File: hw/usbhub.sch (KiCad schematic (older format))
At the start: 0 parts

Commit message: Add more
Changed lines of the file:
@@
 $Descr A4 11693 8268
 encoding utf-8
-Sheet 1 2
+Sheet 1 4
 Title ""
 Date ""
@@
 F1 "USB2517.sch" 50
 $EndSheet
+$Sheet
+S 5550 2750 1550 2450
+U 5B992EC8
+F0 "USBPorts" 50
+F1 "USBPorts.sch" 50
+$EndSheet
+$Sheet
+S 7550 2750 1250 2400
+U 5B9586FD
+F0 "MCU" 50
+F1 "MCU.sch" 50
+$EndSheet
 $EndSCHEMATC

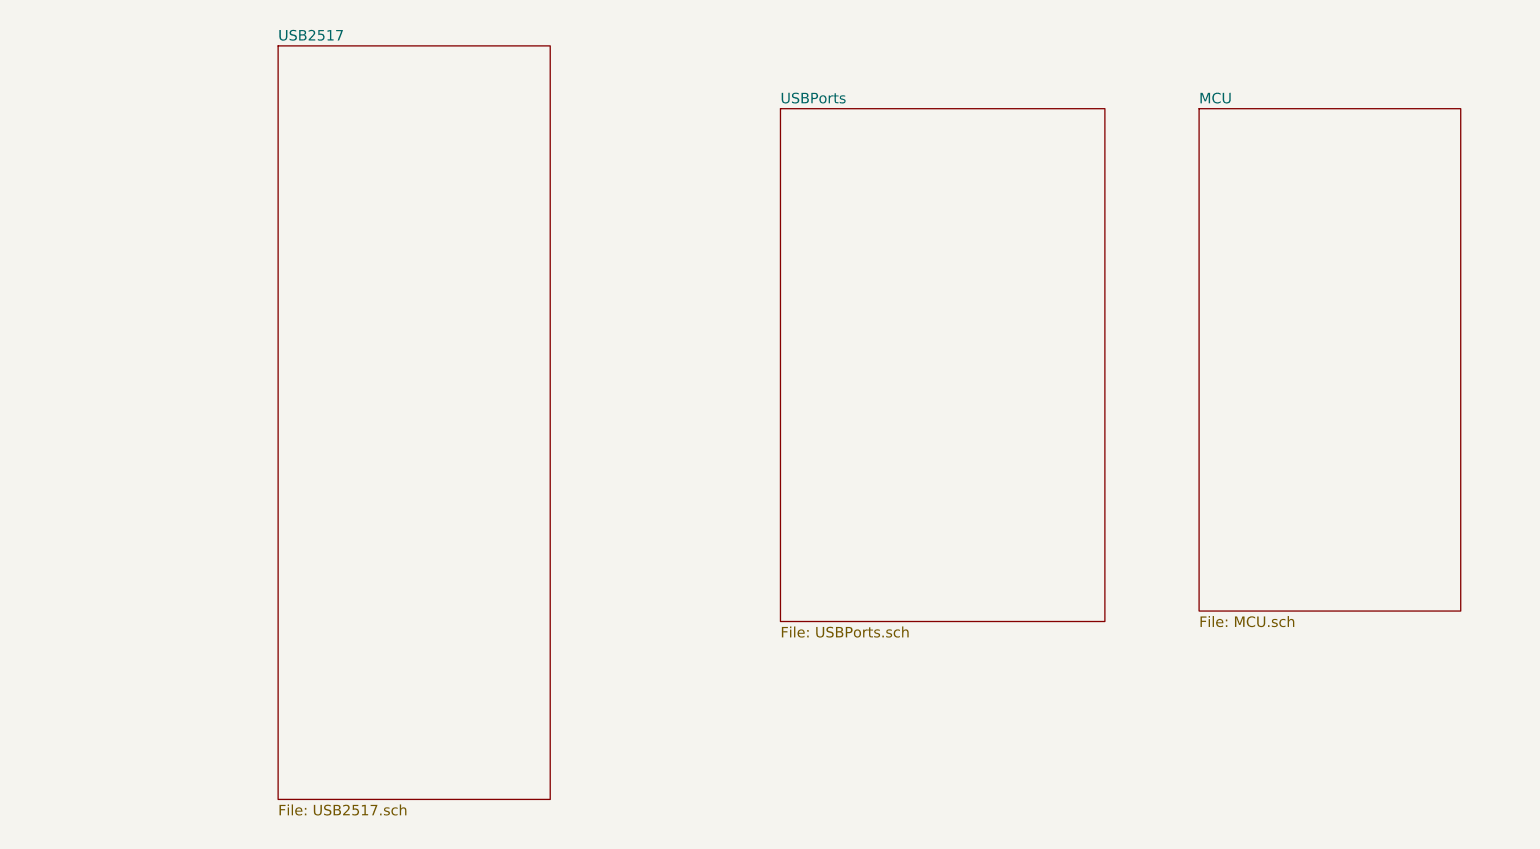
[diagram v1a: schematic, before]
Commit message: Finish up usb port hookup
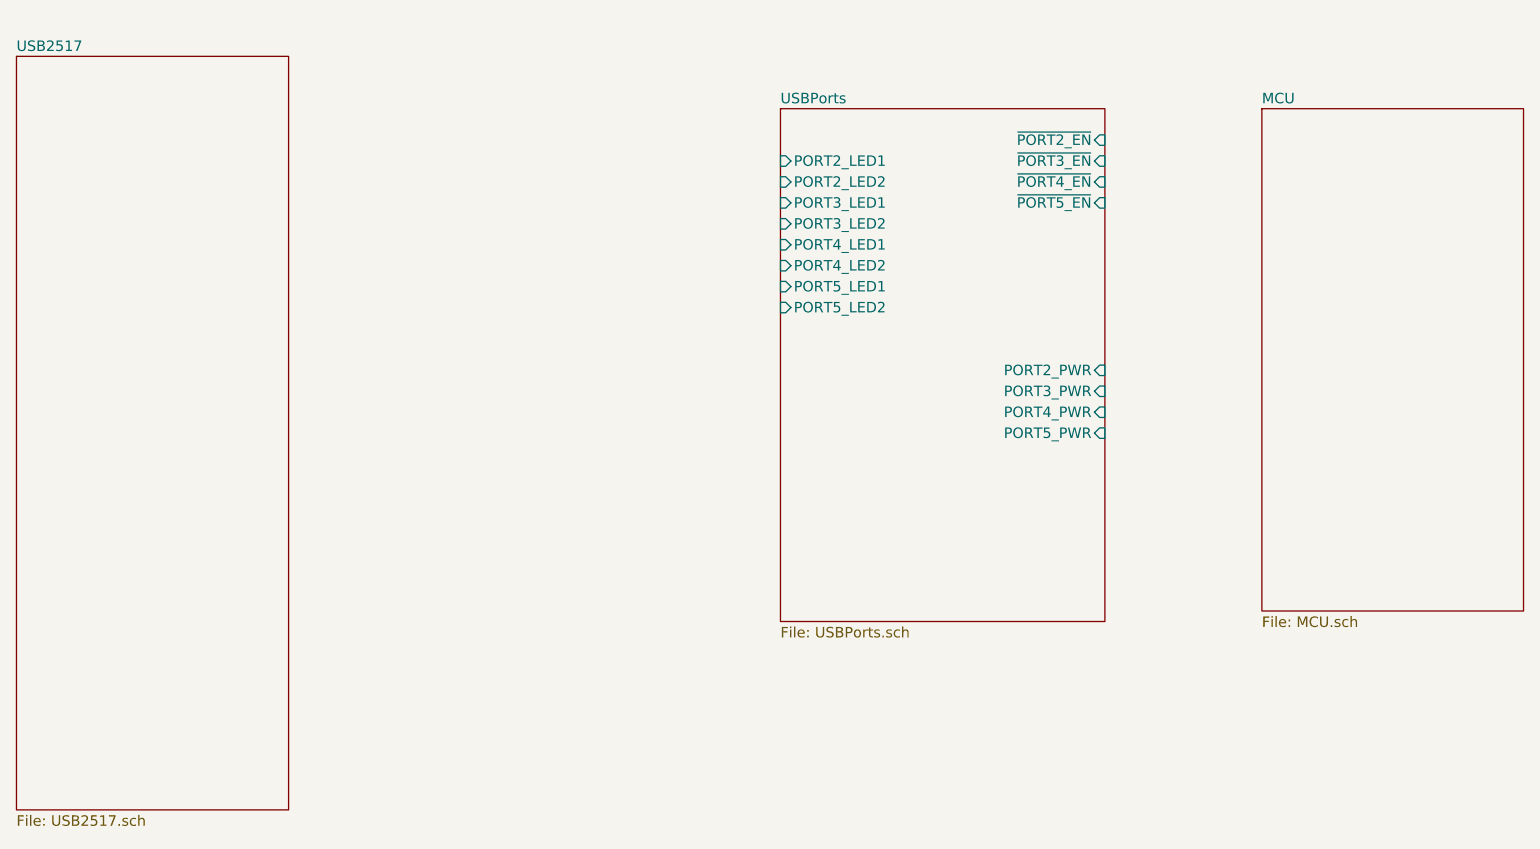
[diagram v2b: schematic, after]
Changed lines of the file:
@@
 $EndDescr
 $Sheet
-S 3150 2450 1300 3600
+S 1900 2500 1300 3600
 U 5A7CEC76
 F0 "USB2517" 50
@@
 F0 "USBPorts" 50
 F1 "USBPorts.sch" 50
+F2 "~PORT3_EN~" I R 7100 3000 50
+F3 "PORT2_LED1" I L 5550 3000 50
+F4 "PORT2_LED2" I L 5550 3100 50
+F5 "PORT2_PWR" I R 7100 4000 50
+F6 "PORT3_LED1" I L 5550 3200 50
+F7 "PORT3_LED2" I L 5550 3300 50
+F8 "PORT3_PWR" I R 7100 4100 50
+F9 "PORT4_LED1" I L 5550 3400 50
+F10 "PORT4_LED2" I L 5550 3500 50
+F11 "PORT4_PWR" I R 7100 4200 50
+F12 "PORT5_LED1" I L 5550 3600 50
+F13 "PORT5_LED2" I L 5550 3700 50
+F14 "PORT5_PWR" I R 7100 4300 50
+F15 "~PORT4_EN~" I R 7100 3100 50
+F16 "~PORT5_EN~" I R 7100 3200 50
+F17 "~PORT2_EN~" I R 7100 2900 50
 $EndSheet
 $Sheet
-S 7550 2750 1250 2400
+S 7850 2750 1250 2400
 U 5B9586FD
 F0 "MCU" 50

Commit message: Finalize schematics
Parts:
- added R21, R22, R23, R24, R25, R26, R27, R28: 360R, symbol Device:R_Small
- added U12, U13, U14, U15: LED_GRAB, symbol LED_Extra:LED_GRAB
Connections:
- net labels added: +3V3
- wire segments 0 -> 49
- no-connect marks 0 -> 4

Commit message: Add most footprints, switch to usb c
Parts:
- R21, R22, R23, R24, R25, R26, R27, R28: footprint (none) -> Resistor_SMD:R_0603_1608Metric
- U12, U13, U14, U15: footprint (none) -> LED_SMD_Extra:LED_RGB_0606_1616Metric
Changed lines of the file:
@@
 F 0 "U12" H 4700 2433 50  0000 C CNN
 F 1 "LED_GRAB" H 4700 2524 50  0000 C CNN
-F 2 "" H 4750 2900 50  0001 C CNN
+F 2 "LED_SMD_Extra:LED_RGB_0606_1616Metric" H 4750 2900 50  0001 C CNN
 F 3 "" H 4750 2900 50  0001 C CNN
 	1    4750 2900
@@
 F 0 "U13" H 4700 3183 50  0000 C CNN
 F 1 "LED_GRAB" H 4700 3274 50  0000 C CNN
-F 2 "" H 4750 3650 50  0001 C CNN
+F 2 "LED_SMD_Extra:LED_RGB_0606_1616Metric" H 4750 3650 50  0001 C CNN
 F 3 "" H 4750 3650 50  0001 C CNN
 	1    4750 3650
@@
 F 0 "U14" H 4700 3833 50  0000 C CNN
 F 1 "LED_GRAB" H 4700 3924 50  0000 C CNN
-F 2 "" H 4750 4300 50  0001 C CNN
+F 2 "LED_SMD_Extra:LED_RGB_0606_1616Metric" H 4750 4300 50  0001 C CNN
 F 3 "" H 4750 4300 50  0001 C CNN
 	1    4750 4300
@@
 F 0 "U15" H 4700 4483 50  0000 C CNN
 F 1 "LED_GRAB" H 4700 4574 50  0000 C CNN
-F 2 "" H 4750 4950 50  0001 C CNN
+F 2 "LED_SMD_Extra:LED_RGB_0606_1616Metric" H 4750 4950 50  0001 C CNN
 F 3 "" H 4750 4950 50  0001 C CNN
 	1    4750 4950
@@
 F 0 "R21" V 5150 2900 50  0000 C CNN
 F 1 "360R" V 5045 2900 50  0000 C CNN
-F 2 "" H 5150 2900 50  0001 C CNN
+F 2 "Resistor_SMD:R_0603_1608Metric" H 5150 2900 50  0001 C CNN
 F 3 "~" H 5150 2900 50  0001 C CNN
 	1    5150 2900
@@
 F 0 "R22" V 5150 3100 50  0000 C CNN
 F 1 "360R" V 5250 3100 50  0000 C CNN
-F 2 "" H 5150 3100 50  0001 C CNN
+F 2 "Resistor_SMD:R_0603_1608Metric" H 5150 3100 50  0001 C CNN
 F 3 "~" H 5150 3100 50  0001 C CNN
 	1    5150 3100
@@
 F 0 "R23" V 5150 3650 50  0000 C CNN
 F 1 "360R" V 5045 3650 50  0000 C CNN
-F 2 "" H 5150 3650 50  0001 C CNN
+F 2 "Resistor_SMD:R_0603_1608Metric" H 5150 3650 50  0001 C CNN
 F 3 "~" H 5150 3650 50  0001 C CNN
 	1    5150 3650
@@
 F 0 "R24" V 5150 3850 50  0000 C CNN
 F 1 "360R" V 5250 3850 50  0000 C CNN
-F 2 "" H 5150 3850 50  0001 C CNN
+F 2 "Resistor_SMD:R_0603_1608Metric" H 5150 3850 50  0001 C CNN
 F 3 "~" H 5150 3850 50  0001 C CNN
 	1    5150 3850
@@
 F 0 "R25" V 5150 4300 50  0000 C CNN
 F 1 "360R" V 5045 4300 50  0000 C CNN
-F 2 "" H 5150 4300 50  0001 C CNN
+F 2 "Resistor_SMD:R_0603_1608Metric" H 5150 4300 50  0001 C CNN
 F 3 "~" H 5150 4300 50  0001 C CNN
 	1    5150 4300
@@
 F 0 "R26" V 5150 4500 50  0000 C CNN
 F 1 "360R" V 5250 4500 50  0000 C CNN
-F 2 "" H 5150 4500 50  0001 C CNN
+F 2 "Resistor_SMD:R_0603_1608Metric" H 5150 4500 50  0001 C CNN
 F 3 "~" H 5150 4500 50  0001 C CNN
 	1    5150 4500
@@
 F 0 "R27" V 5150 4950 50  0000 C CNN
 F 1 "360R" V 5045 4950 50  0000 C CNN
-F 2 "" H 5150 4950 50  0001 C CNN
+F 2 "Resistor_SMD:R_0603_1608Metric" H 5150 4950 50  0001 C CNN
 F 3 "~" H 5150 4950 50  0001 C CNN
 	1    5150 4950
@@
 F 0 "R28" V 5150 5150 50  0000 C CNN
 F 1 "360R" V 5250 5150 50  0000 C CNN
-F 2 "" H 5150 5150 50  0001 C CNN
+F 2 "Resistor_SMD:R_0603_1608Metric" H 5150 5150 50  0001 C CNN
 F 3 "~" H 5150 5150 50  0001 C CNN
 	1    5150 5150

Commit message: More placement, more issues
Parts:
- removed R21, R22, R23, R24, R25, R26, R27, R28: 360R, Resistor_SMD:R_0603_1608Metric, symbol Device:R_Small
- removed U12, U13, U14, U15: LED_GRAB, LED_SMD_Extra:LED_RGB_0606_1616Metric, symbol LED_Extra:LED_GRAB
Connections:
- net labels removed: +3V3
- wire segments 49 -> 8
- no-connect marks 4 -> 0
